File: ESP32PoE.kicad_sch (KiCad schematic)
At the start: 4 parts

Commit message: chore: add README (#2)
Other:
- title: (none) -> ESP32 PoE
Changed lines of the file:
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@@
 	(generator_version "9.0")
 	(paper "A4")
+	(title_block
+		(title "ESP32 PoE")
+		(rev "v0.1.0")
+	)
 	(bus
 		(pts

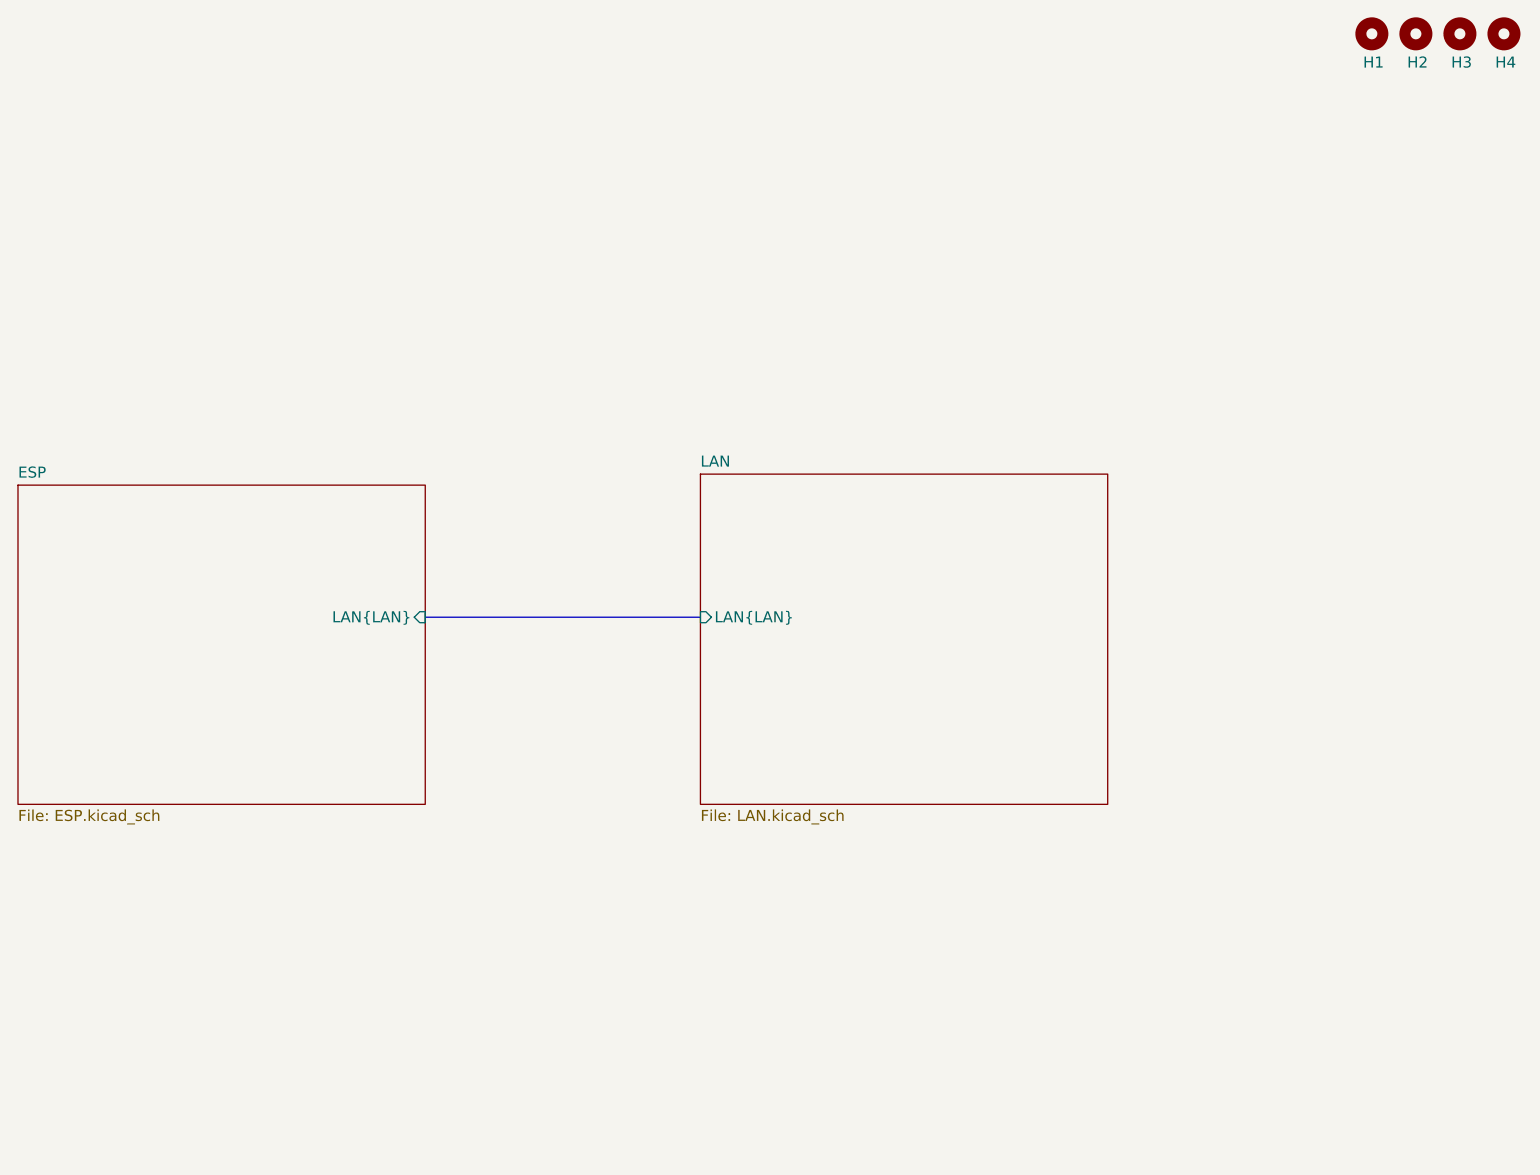
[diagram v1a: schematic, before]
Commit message: feat: redesign to smaller form factor
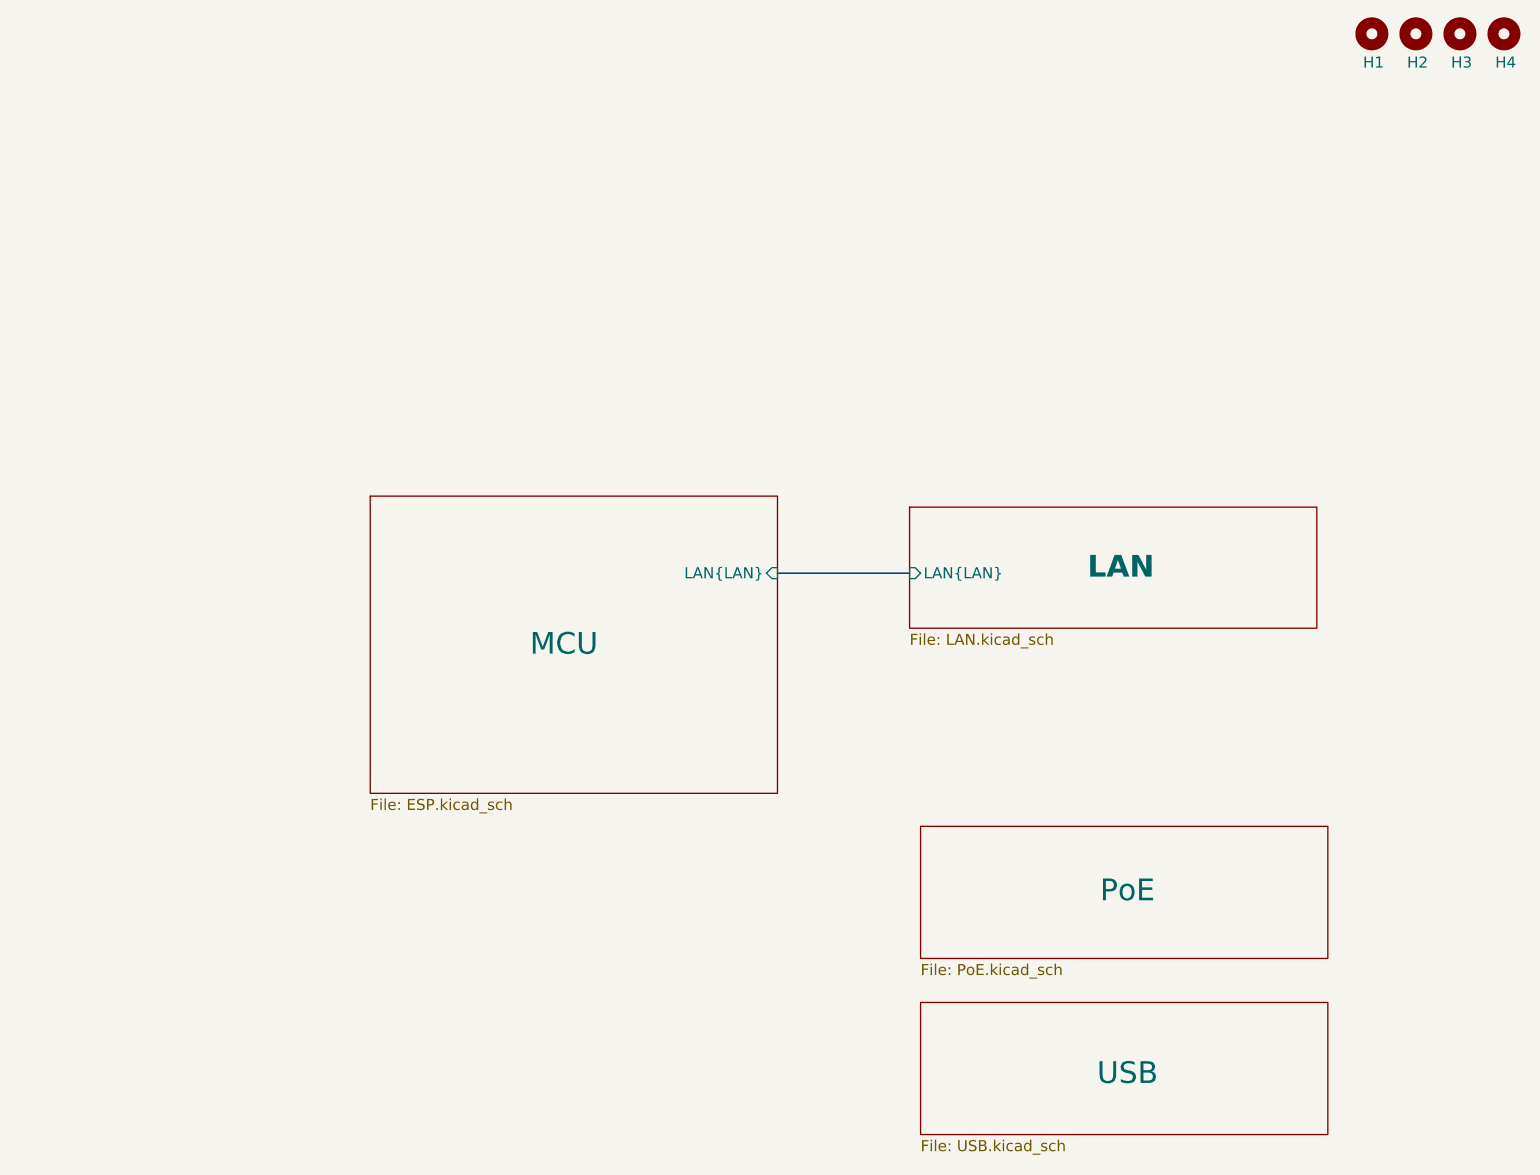
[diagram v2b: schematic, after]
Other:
- sheet ESP renamed MCU
- added sheet PoE (PoE.kicad_sch)
- added sheet USB (USB.kicad_sch)
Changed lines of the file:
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@@
 	(title_block
 		(title "ESP32 PoE")
-		(rev "v0.1.0")
+		(rev "v0.2.0")
 	)
 	(bus
 		(pts
-			(xy 125.73 85.09) (xy 157.48 85.09)
+			(xy 166.37 80.01) (xy 181.61 80.01)
 		)
 		(stroke
@@
 	)
 	(sheet
-		(at 78.74 69.85)
-		(size 46.99 36.83)
+		(at 182.88 109.22)
+		(size 46.99 15.24)
 		(exclude_from_sim no)
 		(in_bom yes)
 		(on_board yes)
 		(dnp no)
-		(fields_autoplaced yes)
 		(stroke
 			(width 0.1524)
@@
 			(color 0 0 0 0.0000)
 		)
-		(property "Sheetname" "ESP"
-			(at 78.74 69.1384 0)
-			(effects
-				(font
-					(size 1.27 1.27)
-				)
-				(justify left bottom)
-			)
-		)
-		(property "Sheetfile" "ESP.kicad_sch"
-			(at 78.74 107.2646 0)
+		(property "Sheetname" "PoE"
+			(at 206.756 116.586 0)
+			(effects
+				(font
+					(size 2.5 2.5)
+					(thickness 0.3125)
+				)
+			)
+		)
+		(property "Sheetfile" "PoE.kicad_sch"
+			(at 182.88 125.0446 0)
 			(effects
 				(font
@@
 			)
 		)
-		(pin "LAN{LAN}" input
-			(at 125.73 85.09 0)
-			(effects
-				(font
-					(size 1.27 1.27)
-				)
-				(justify right)
-			)
-		)
-		(instances
-			(project "ESP32PoE"
-				(path "/d24e1617-e618-4b3e-afdf-d73937c6f436"
-					(page "3")
+		(instances
+			(project "ESP32PoE"
+				(path "/d24e1617-e618-4b3e-afdf-d73937c6f436"
+					(page "4")
 				)
 			)
@@
 	)
 	(sheet
-		(at 157.48 68.58)
-		(size 46.99 38.1)
+		(at 182.88 129.54)
+		(size 46.99 15.24)
 		(exclude_from_sim no)
 		(in_bom yes)
 		(on_board yes)
 		(dnp no)
-		(fields_autoplaced yes)
 		(stroke
 			(width 0.1524)
@@
 			(color 0 0 0 0.0000)
 		)
+		(property "Sheetname" "USB"
+			(at 206.756 137.668 0)
+			(effects
+				(font
+					(size 2.5 2.5)
+					(thickness 0.3125)
+				)
+			)
+		)
+		(property "Sheetfile" "USB.kicad_sch"
+			(at 182.88 145.3646 0)
+			(effects
+				(font
+					(size 1.27 1.27)
+				)
+				(justify left top)
+			)
+		)
+		(instances
+			(project "ESP32PoE"
+				(path "/d24e1617-e618-4b3e-afdf-d73937c6f436"
+					(page "5")
+				)
+			)
+		)
+	)
+	(sheet
+		(at 119.38 71.12)
+		(size 46.99 34.29)
+		(exclude_from_sim no)
+		(in_bom yes)
+		(on_board yes)
+		(dnp no)
+		(stroke
+			(width 0.1524)
+			(type solid)
+		)
+		(fill
+			(color 0 0 0 0.0000)
+		)
+		(property "Sheetname" "MCU"
+			(at 141.732 88.138 0)
+			(effects
+				(font
+					(size 2.5 2.5)
+					(thickness 0.3125)
+				)
+			)
+		)
+		(property "Sheetfile" "ESP.kicad_sch"
+			(at 119.38 105.9946 0)
+			(effects
+				(font
+					(size 1.27 1.27)
+				)
+				(justify left top)
+			)
+		)
+		(pin "LAN{LAN}" input
+			(at 166.37 80.01 0)
+			(effects
+				(font
+					(size 1.27 1.27)
+				)
+				(justify right)
+			)
+		)
+		(instances
+			(project "ESP32PoE"
+				(path "/d24e1617-e618-4b3e-afdf-d73937c6f436"
+					(page "2")
+				)
+			)
+		)
+	)
+	(sheet
+		(at 181.61 72.39)
+		(size 46.99 13.97)
+		(exclude_from_sim no)
+		(in_bom yes)
+		(on_board yes)
+		(dnp no)
+		(stroke
+			(width 0.1524)
+			(type solid)
+		)
+		(fill
+			(color 0 0 0 0.0000)
+		)
 		(property "Sheetname" "LAN"
-			(at 157.48 67.8684 0)
-			(effects
-				(font
-					(size 1.27 1.27)
-				)
-				(justify left bottom)
+			(at 205.994 79.248 0)
+			(effects
+				(font
+					(size 2.5 2.5)
+					(thickness 0.254)
+					(bold yes)
+				)
 			)
 		)
 		(property "Sheetfile" "LAN.kicad_sch"
-			(at 157.48 107.2646 0)
+			(at 181.61 86.9446 0)
 			(effects
 				(font
@@
 		)
 		(pin "LAN{LAN}" input
-			(at 157.48 85.09 180)
-			(effects
-				(font
-					(size 1.27 1.27)
-				)
-				(justify left)
-			)
-		)
-		(instances
-			(project "ESP32PoE"
-				(path "/d24e1617-e618-4b3e-afdf-d73937c6f436"
-					(page "2")
-				)
-			)
+			(at 181.61 80.01 180)
+			(effects
+				(font
+					(size 1.27 1.27)
+				)
+				(justify left)
+			)
+		)
+		(instances
+			(project "ESP32PoE"
+				(path "/d24e1617-e618-4b3e-afdf-d73937c6f436"
+					(page "3")
+				)
+			)
